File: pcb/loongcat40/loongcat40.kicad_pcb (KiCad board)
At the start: 2 copper layers, 83 parts, among them SW1 SW_Push, SW10 SW_Push, SW11 SW_Push, SW12 SW_Push, SW13 SW_Push, SW14 SW_Push, SW15 SW_Push, SW16 SW_Push, SW17 SW_Push, SW18 SW_Push, SW19 SW_Push, SW2 SW_Push, SW20 SW_Push, SW21 SW_Push, SW22 SW_Push, SW23 SW_Push, SW24 SW_Push, SW25 SW_Push, SW26 SW_Push, SW27 SW_Push, SW28 SW_Push, SW29 SW_Push, SW3 SW_Push, SW30 SW_Push, SW31 SW_Push, SW32 SW_Push, SW33 SW_Push, SW34 SW_Push, SW35 SW_Push, SW36 SW_Push, SW37 SW_Push, SW38 SW_Push, SW39 SW_Push, SW4 SW_Push, SW40 SW_Push, SW5 SW_Push, SW6 SW_Push, SW7 SW_Push, SW8 SW_Push, SW9 SW_Push

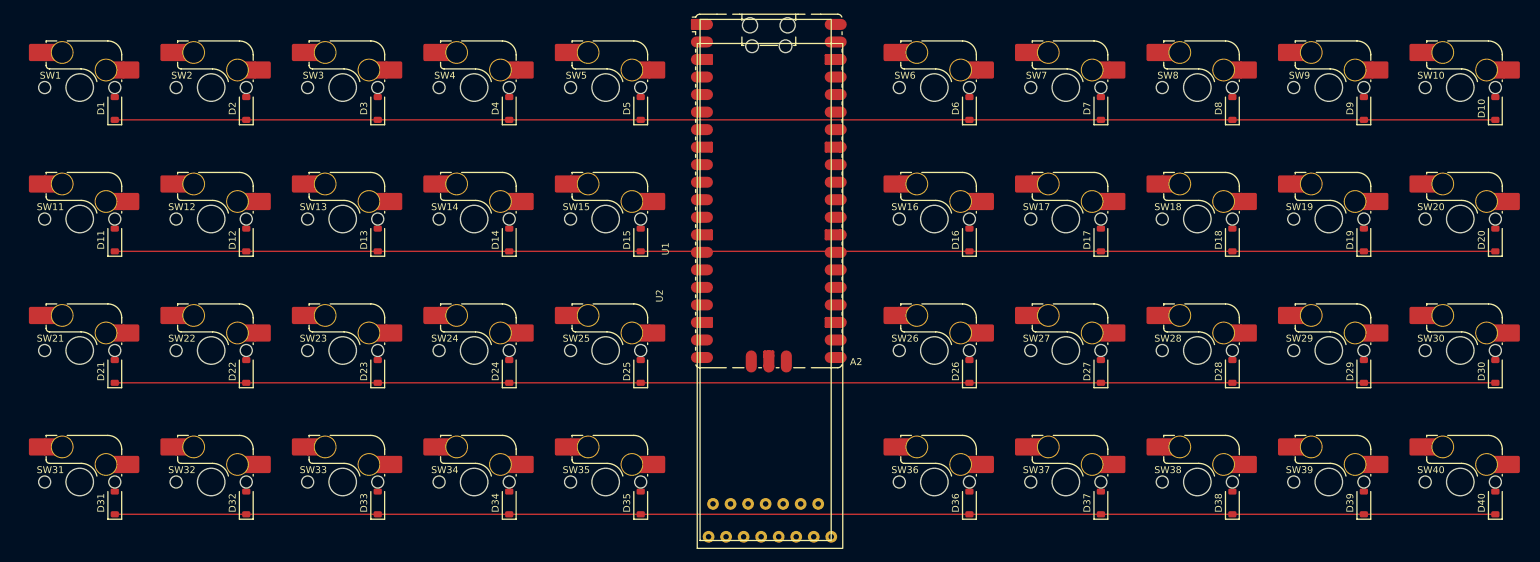
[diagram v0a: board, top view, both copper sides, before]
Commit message: position parts on pcb
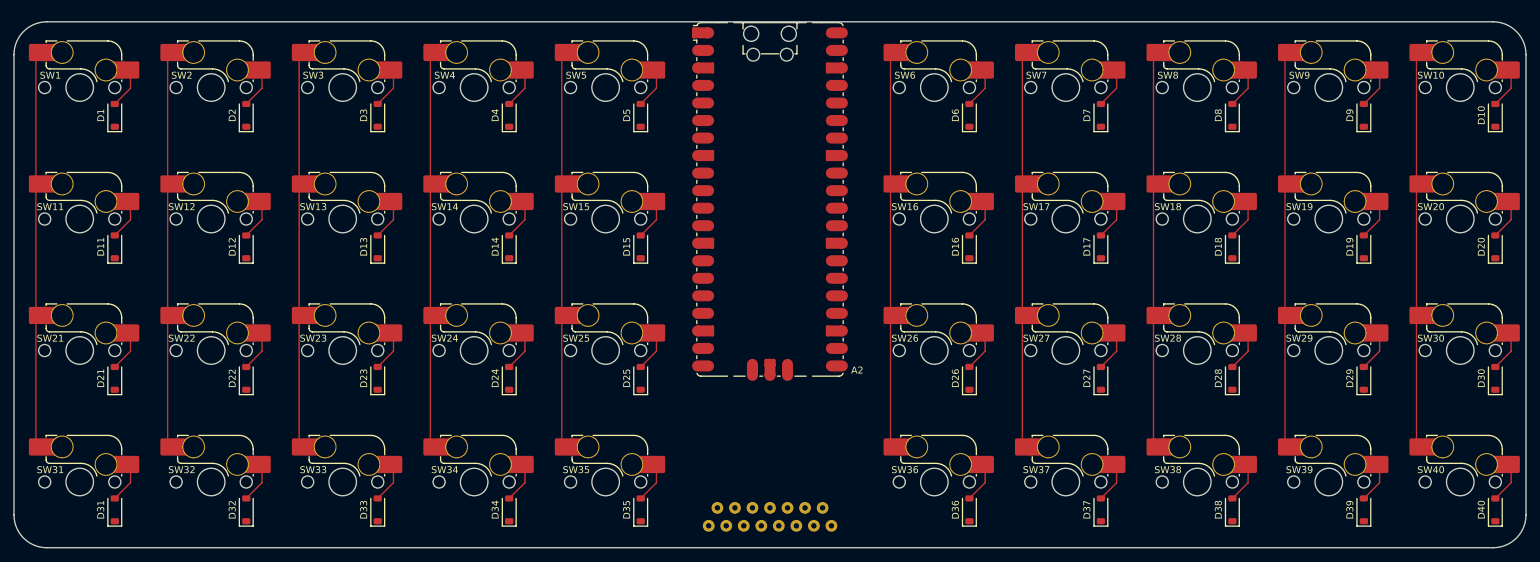
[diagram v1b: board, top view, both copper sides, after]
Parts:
- U1, U2: moved to B.Cu
- moved U2 1.59 mm to (138.1, 66.7)
- moved A2 1.23 mm to (138.1, 54.3)
- moved D1 1.00 mm to (43.2, 42.1)
- moved D10 1.00 mm to (243.2, 42.1)
- moved D11 1.00 mm to (43.2, 61.2)
- moved D12 1.00 mm to (62.2, 61.2)
- moved D13 1.00 mm to (81.3, 61.2)
- moved D14 1.00 mm to (100.3, 61.2)
- moved D15 1.00 mm to (119.4, 61.2)
- moved D16 1.00 mm to (167.0, 61.2)
- moved D17 1.00 mm to (186.1, 61.2)
- moved D18 1.00 mm to (205.1, 61.2)
- moved D19 1.00 mm to (224.2, 61.2)
- moved D2 1.00 mm to (62.2, 42.1)
- moved D20 1.00 mm to (243.2, 61.2)
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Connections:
- A2 pad 1: unconnected-(A2-GPIO0-Pad1) -> COL_1
- A2 pad 10: unconnected-(A2-GPIO7-Pad10) -> ROW_2
- A2 pad 11: unconnected-(A2-GPIO8-Pad11) -> ROW_3
- A2 pad 12: unconnected-(A2-GPIO9-Pad12) -> ROW_4
- A2 pad 19: unconnected-(A2-GPIO14-Pad19) -> RST
- A2 pad 2: unconnected-(A2-GPIO1-Pad2) -> COL_2
- A2 pad 20: unconnected-(A2-GPIO15-Pad20) -> DC
- A2 pad 22: unconnected-(A2-GPIO17-Pad22) -> CS
- A2 pad 24: unconnected-(A2-GPIO18-Pad24) -> SCL
- A2 pad 25: unconnected-(A2-GPIO19-Pad25) -> SDA
- A2 pad 26: unconnected-(A2-GPIO20-Pad26) -> COL_10
- A2 pad 27: unconnected-(A2-GPIO21-Pad27) -> COL_9
- A2 pad 29: unconnected-(A2-GPIO22-Pad29) -> COL_8
- A2 pad 31: unconnected-(A2-GPIO26_ADC0-Pad31) -> COL_7
- A2 pad 32: unconnected-(A2-GPIO27_ADC1-Pad32) -> COL_6
- A2 pad 4: unconnected-(A2-GPIO2-Pad4) -> COL_3
- A2 pad 5: unconnected-(A2-GPIO3-Pad5) -> COL_4
- A2 pad 6: unconnected-(A2-GPIO4-Pad6) -> COL_5
- A2 pad 9: unconnected-(A2-GPIO6-Pad9) -> ROW_1
- U2 pad 8: unconnected-(U2-BL-Pad8) -> BL
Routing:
- net ROW_4: track 200.0 -> 0.00 mm
- net ROW_2: track 200.0 -> 0.00 mm
- net ROW_3: track 200.0 -> 0.00 mm
- net ROW_1: track 200.0 -> 0.00 mm
- net COL_9: track 0.00 -> 57.4 mm
- net COL_6: track 0.00 -> 57.4 mm
- net COL_1: track 0.00 -> 57.4 mm
- net COL_8: track 0.00 -> 57.4 mm
- net COL_4: track 0.00 -> 57.4 mm
- net COL_10: track 0.00 -> 57.4 mm
- net COL_5: track 0.00 -> 57.4 mm
- net COL_2: track 0.00 -> 57.3 mm
- net COL_3: track 0.00 -> 57.3 mm
- net COL_7: track 0.00 -> 57.3 mm
- net Net-(D32-A): track 0.00 -> 5.86 mm
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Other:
- board outline added: 219.1 x 76.2 mm

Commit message: create outputs; init keyboard case
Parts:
- added H1: MountingHole_Pad, MountingHole:MountingHole_2.2mm_M2_Pad, F.Cu at (47.6, 47.6)
- added H2: MountingHole_Pad, MountingHole:MountingHole_2.2mm_M2_Pad, F.Cu at (228.6, 47.6)
- added H3: MountingHole_Pad, MountingHole:MountingHole_2.2mm_M2_Pad, F.Cu at (104.8, 66.7)
- added H4: MountingHole_Pad, MountingHole:MountingHole_2.2mm_M2_Pad, F.Cu at (171.4, 66.7)
- added H5: MountingHole_Pad, MountingHole:MountingHole_2.2mm_M2_Pad, F.Cu at (47.6, 85.7)
- added H6: MountingHole_Pad, MountingHole:MountingHole_2.2mm_M2_Pad, F.Cu at (228.6, 85.7)
- U2: moved to F.Cu
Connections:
- A2 pad 17: unconnected-(A2-GPIO13-Pad17) -> BL
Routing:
- net ROW_4: track 0.00 -> 272.5 mm, vias 0 -> 10
- net ROW_3: track 0.00 -> 256.3 mm, vias 0 -> 10
- net ROW_2: track 0.00 -> 239.0 mm, vias 0 -> 10
- net ROW_1: track 0.00 -> 232.8 mm, vias 0 -> 11
- net COL_1: track 57.4 -> 157.0 mm, vias 0 -> 2
- net COL_10: track 57.4 -> 144.2 mm, vias 0 -> 2
- net COL_2: track 57.3 -> 138.1 mm, vias 0 -> 2
- net COL_9: track 57.4 -> 122.4 mm, vias 0 -> 2
- net +3.3V: track 0.00 -> 63.2 mm, vias 0 -> 2
- net CS: track 0.00 -> 61.5 mm, vias 0 -> 4
- net BL: track 0.00 -> 60.2 mm, vias 0 -> 2
- net COL_3: track 57.3 -> 117.3 mm, vias 0 -> 2
- net SCL: track 0.00 -> 49.7 mm, vias 0 -> 4
- net COL_8: track 57.4 -> 104.1 mm, vias 0 -> 2
- net SDA: track 0.00 -> 44.5 mm, vias 0 -> 2
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- added copper zone on B.Cu, net +3.3V
- added copper zone on F.Cu, net GND
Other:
- board text added: "GND"
- board text added: "loongcat is looooooooooooooooooooooooooooooooooooooooooooooooooooooooooooooooooooooooooooooooooooooooooooooooooooooooooooooooooooooooooooooooooooooooooooooong"
- board text added: "loongcat40 v0.0 by sporewoh"

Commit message: update pcb to v0.1
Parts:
- added SW41: SW_Push, keyswitches:Kailh_socket_MX, B.Cu at (104.8, 95.2)
- added SW42: SW_Push, keyswitches:Kailh_socket_MX, B.Cu at (171.4, 95.2)
- A2: footprint Module:RaspberryPi_Pico_SMD_HandSolder -> Module:RaspberryPi_Pico_Common_Unspecified
- SW1, SW10, SW11, SW12, SW13, SW14, SW15, SW16, SW17, SW18, SW19, SW2, SW20, SW21, SW22, SW23, SW24, SW25, SW26, SW27, SW28, SW29, SW3, SW30, SW31, SW32, SW33, SW34, SW35, SW36, SW37, SW38, SW39, SW4, SW40, SW5, SW6, SW7, SW8, SW9: footprint marbastlib-mx:SW_MX_HS_CPG151101S11_1u -> keyswitches:Kailh_socket_MX; moved to B.Cu
- moved D34 9.84 mm to (90.5, 99.3)
- moved D36 8.25 mm to (158.8, 99.3)
- turned SW1 to 180 degrees
- turned SW10 to 180 degrees
- turned SW11 to 180 degrees
- turned SW12 to 180 degrees
- turned SW13 to 180 degrees
- turned SW14 to 180 degrees
- turned SW15 to 180 degrees
- turned SW16 to 180 degrees
- turned SW17 to 180 degrees
- turned SW18 to 180 degrees
- turned SW19 to 180 degrees
- turned SW2 to 180 degrees
- turned SW20 to 180 degrees
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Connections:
- SW1 pad 1: Net-(D1-A) -> COL_1
- SW1 pad 2: COL_1 -> Net-(D1-A)
- SW10 pad 1: Net-(D10-A) -> COL_10
- SW10 pad 2: COL_10 -> Net-(D10-A)
- SW11 pad 1: Net-(D11-A) -> COL_1
- SW11 pad 2: COL_1 -> Net-(D11-A)
- SW12 pad 1: Net-(D12-A) -> COL_2
- SW12 pad 2: COL_2 -> Net-(D12-A)
- SW13 pad 1: Net-(D13-A) -> COL_3
- SW13 pad 2: COL_3 -> Net-(D13-A)
- SW14 pad 1: Net-(D14-A) -> COL_4
- SW14 pad 2: COL_4 -> Net-(D14-A)
- SW15 pad 1: Net-(D15-A) -> COL_5
- SW15 pad 2: COL_5 -> Net-(D15-A)
- SW16 pad 1: Net-(D16-A) -> COL_6
- SW16 pad 2: COL_6 -> Net-(D16-A)
- SW17 pad 1: Net-(D17-A) -> COL_7
- SW17 pad 2: COL_7 -> Net-(D17-A)
- SW18 pad 1: Net-(D18-A) -> COL_8
- SW18 pad 2: COL_8 -> Net-(D18-A)
- SW19 pad 1: Net-(D19-A) -> COL_9
- SW19 pad 2: COL_9 -> Net-(D19-A)
- SW2 pad 1: Net-(D2-A) -> COL_2
- SW2 pad 2: COL_2 -> Net-(D2-A)
- SW20 pad 1: Net-(D20-A) -> COL_10
- SW20 pad 2: COL_10 -> Net-(D20-A)
- SW21 pad 1: Net-(D21-A) -> COL_1
- SW21 pad 2: COL_1 -> Net-(D21-A)
- SW22 pad 1: Net-(D22-A) -> COL_2
- SW22 pad 2: COL_2 -> Net-(D22-A)
- SW23 pad 1: Net-(D23-A) -> COL_3
- SW23 pad 2: COL_3 -> Net-(D23-A)
- SW24 pad 1: Net-(D24-A) -> COL_4
- SW24 pad 2: COL_4 -> Net-(D24-A)
- SW25 pad 1: Net-(D25-A) -> COL_5
- SW25 pad 2: COL_5 -> Net-(D25-A)
- SW26 pad 1: Net-(D26-A) -> COL_6
- SW26 pad 2: COL_6 -> Net-(D26-A)
- SW27 pad 1: Net-(D27-A) -> COL_7
- SW27 pad 2: COL_7 -> Net-(D27-A)
- SW28 pad 1: Net-(D28-A) -> COL_8
- SW28 pad 2: COL_8 -> Net-(D28-A)
- SW29 pad 1: Net-(D29-A) -> COL_9
- SW29 pad 2: COL_9 -> Net-(D29-A)
- SW3 pad 1: Net-(D3-A) -> COL_3
- SW3 pad 2: COL_3 -> Net-(D3-A)
- SW30 pad 1: Net-(D30-A) -> COL_10
- SW30 pad 2: COL_10 -> Net-(D30-A)
- SW31 pad 1: Net-(D31-A) -> COL_1
- SW31 pad 2: COL_1 -> Net-(D31-A)
- SW32 pad 1: Net-(D32-A) -> COL_2
- SW32 pad 2: COL_2 -> Net-(D32-A)
- SW33 pad 1: Net-(D33-A) -> COL_3
- SW33 pad 2: COL_3 -> Net-(D33-A)
- SW34 pad 1: Net-(D34-A) -> COL_4
- SW34 pad 2: COL_4 -> Net-(D34-A)
- SW35 pad 1: Net-(D35-A) -> COL_5
- SW35 pad 2: COL_5 -> Net-(D35-A)
- SW36 pad 1: Net-(D36-A) -> COL_6
- SW36 pad 2: COL_6 -> Net-(D36-A)
- SW37 pad 1: Net-(D37-A) -> COL_7
- SW37 pad 2: COL_7 -> Net-(D37-A)
- SW38 pad 1: Net-(D38-A) -> COL_8
- SW38 pad 2: COL_8 -> Net-(D38-A)
- SW39 pad 1: Net-(D39-A) -> COL_9
- SW39 pad 2: COL_9 -> Net-(D39-A)
- SW4 pad 1: Net-(D4-A) -> COL_4
- SW4 pad 2: COL_4 -> Net-(D4-A)
- SW40 pad 1: Net-(D40-A) -> COL_10
- SW40 pad 2: COL_10 -> Net-(D40-A)
- SW5 pad 1: Net-(D5-A) -> COL_5
- SW5 pad 2: COL_5 -> Net-(D5-A)
- SW6 pad 1: Net-(D6-A) -> COL_6
- SW6 pad 2: COL_6 -> Net-(D6-A)
- SW7 pad 1: Net-(D7-A) -> COL_7
- SW7 pad 2: COL_7 -> Net-(D7-A)
- SW8 pad 1: Net-(D8-A) -> COL_8
- SW8 pad 2: COL_8 -> Net-(D8-A)
- SW9 pad 1: Net-(D9-A) -> COL_9
- SW9 pad 2: COL_9 -> Net-(D9-A)
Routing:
- net COL_6: track 66.3 -> 98.9 mm, vias 2 -> 4
- net Net-(D35-A): track 5.86 -> 29.6 mm, vias 0 -> 2
- net Net-(D36-A): track 5.86 -> 19.1 mm
- net COL_5: track 78.5 -> 89.9 mm
- net Net-(D34-A): track 5.86 -> 16.4 mm
- net GND: track 2.01 -> 0.00 mm
- net ROW_1: track 232.8 -> 233.5 mm
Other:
- board text added: "loongcat40 v0.1 by sporewoh"
- board text removed: "loongcat40 v0.0 by sporewoh"

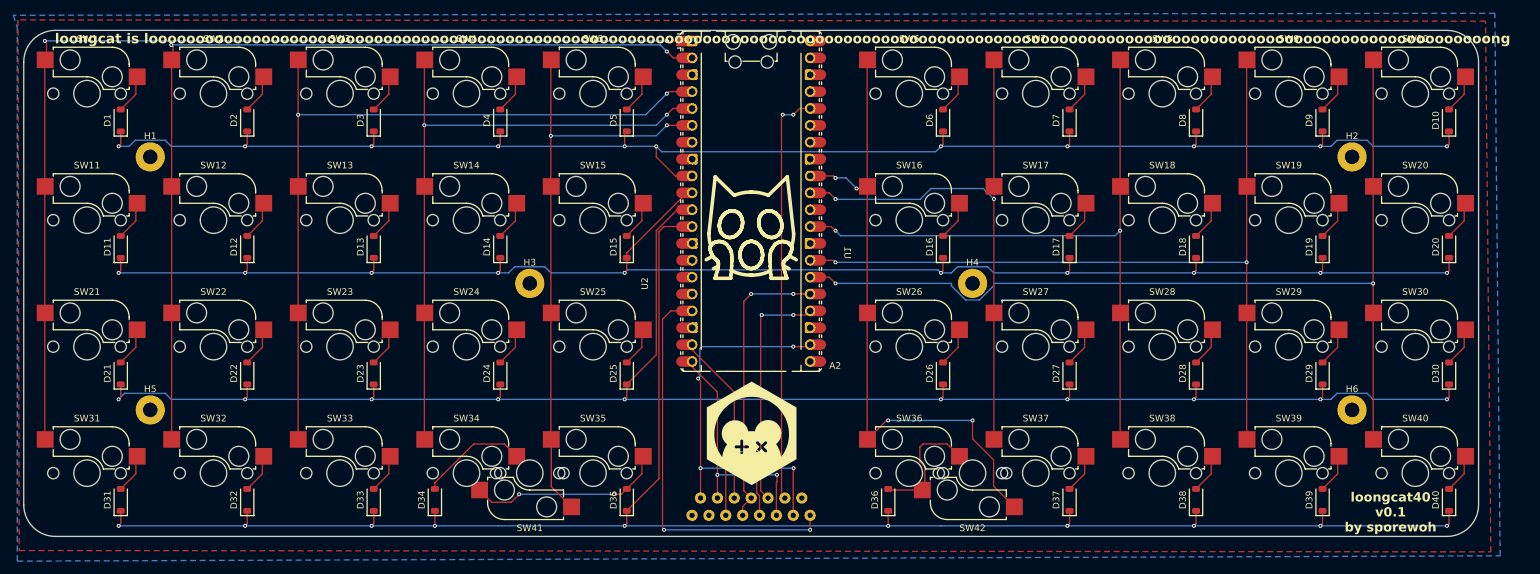
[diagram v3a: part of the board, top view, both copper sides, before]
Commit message: reduce ground plane
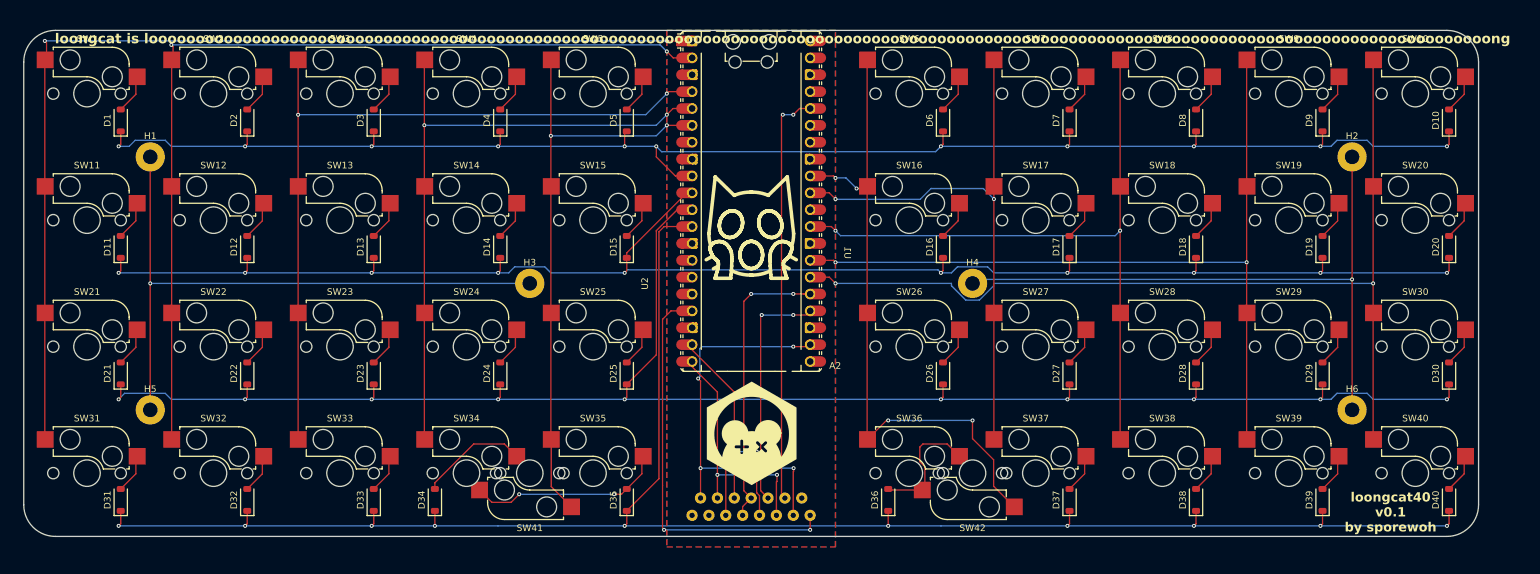
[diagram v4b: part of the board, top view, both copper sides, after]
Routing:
- net GND: track 0.00 -> 190.7 mm, vias 0 -> 2
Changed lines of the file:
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@@
 	)
 	(segment
+		(start 228.6 47.625)
+		(end 228.6 85.725)
+		(width 0.2)
+		(layer "F.Cu")
+		(net 1)
+	)
+	(segment
+		(start 47.625 47.625)
+		(end 47.625 66.675)
+		(width 0.2)
+		(layer "F.Cu")
+		(net 1)
+	)
+	(segment
+		(start 47.625 66.675)
+		(end 47.625 85.725)
+		(width 0.2)
+		(layer "F.Cu")
+		(net 1)
+	)
+	(via
+		(at 228.6 66.075)
+		(size 0.6)
+		(drill 0.3)
+		(layers "F.Cu" "B.Cu")
+		(net 1)
+	)
+	(via
+		(at 47.625 66.675)
+		(size 0.6)
+		(drill 0.3)
+		(layers "F.Cu" "B.Cu")
+		(net 1)
+	)
+	(segment
+		(start 172.05 66.075)
+		(end 228.6 66.075)
+		(width 0.2)
+		(layer "B.Cu")
+		(net 1)
+	)
+	(segment
+		(start 104.775 66.675)
+		(end 47.625 66.675)
+		(width 0.2)
+		(layer "B.Cu")
+		(net 1)
+	)
+	(segment
+		(start 171.45 66.675)
+		(end 172.05 66.075)
+		(width 0.2)
+		(layer "B.Cu")
+		(net 1)
+	)
+	(segment
 		(start 142.683519 98.491019)
 		(end 143.1925 99)
@@
 		(polygon
 			(pts
-				(xy 27.7 27) (xy 27.9 106.9) (xy 249.5 107.1) (xy 248.7 27.2)
+				(xy 125.4125 28.575) (xy 125.4125 106.3625) (xy 150.8125 106.3625) (xy 150.8125 28.575)
 			)
 		)
@@
 		(polygon
 			(pts
-				(xy 27.6 28.1) (xy 27.6 108.5) (xy 250.9 107.7) (xy 250.1 26) (xy 27 26.3)
+				(xy 125.4125 28.575) (xy 125.4125 106.3625) (xy 150.8125 106.3625) (xy 150.8125 28.575) (xy 125.4125 28.575)
 			)
 		)

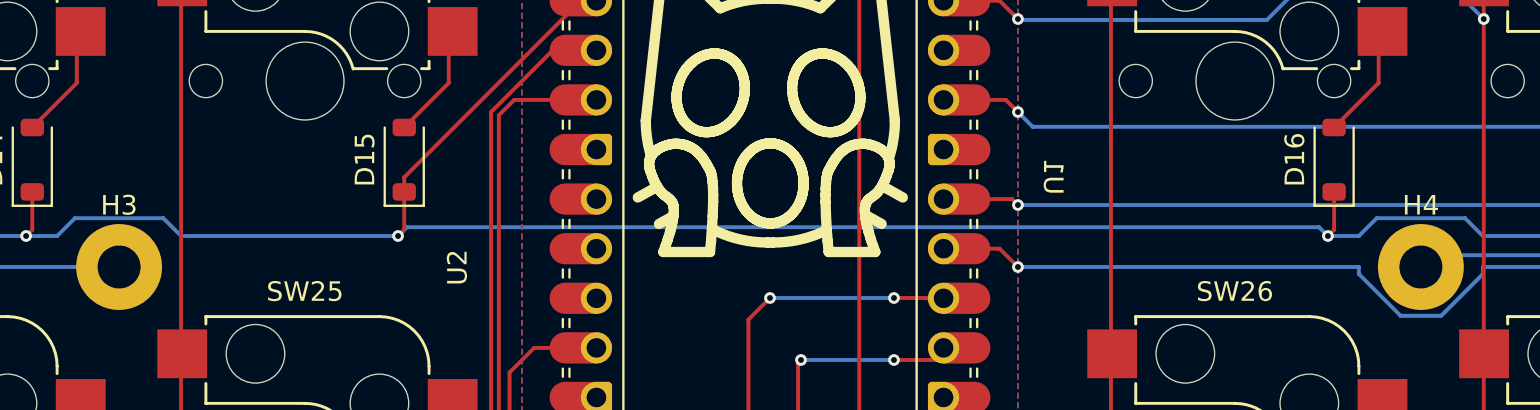
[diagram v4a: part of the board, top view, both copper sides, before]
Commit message: connect ground holes to pico
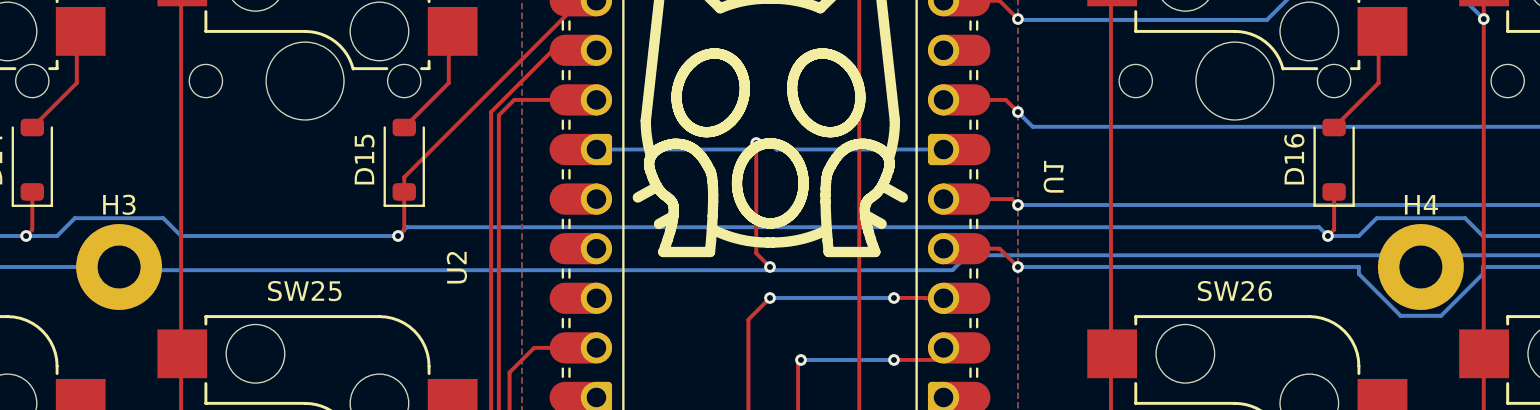
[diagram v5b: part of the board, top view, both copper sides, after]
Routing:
- net GND: track 190.7 -> 282.9 mm, vias 2 -> 4
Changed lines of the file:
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@@
 		(net 1)
 	)
+	(segment
+		(start 138.1125 66.675)
+		(end 137.4092 65.9717)
+		(width 0.2)
+		(layer "F.Cu")
+		(net 1)
+	)
+	(segment
+		(start 137.4092 65.9717)
+		(end 137.4092 60.324764)
+		(width 0.2)
+		(layer "F.Cu")
+		(net 1)
+	)
+	(via
+		(at 138.1125 66.675)
+		(size 0.6)
+		(drill 0.3)
+		(layers "F.Cu" "B.Cu")
+		(net 1)
+	)
 	(via
 		(at 228.6 66.075)
@@
 		(net 1)
 	)
+	(via
+		(at 137.4092 60.324764)
+		(size 0.6)
+		(drill 0.3)
+		(layers "F.Cu" "B.Cu")
+		(net 1)
+	)
+	(segment
+		(start 138.112264 60.324764)
+		(end 138.445 60.6575)
+		(width 0.2)
+		(layer "B.Cu")
+		(net 1)
+	)
+	(segment
+		(start 129.2225 60.6575)
+		(end 137.076464 60.6575)
+		(width 0.2)
+		(layer "B.Cu")
+		(net 1)
+	)
+	(segment
+		(start 138.1125 66.675)
+		(end 137.949 66.8385)
+		(width 0.2)
+		(layer "B.Cu")
+		(net 1)
+	)
 	(segment
 		(start 172.05 66.075)
@@
 	)
 	(segment
+		(start 104.9385 66.8385)
+		(end 104.775 66.675)
+		(width 0.2)
+		(layer "B.Cu")
+		(net 1)
+	)
+	(segment
+		(start 137.076464 60.6575)
+		(end 137.4092 60.324764)
+		(width 0.2)
+		(layer "B.Cu")
+		(net 1)
+	)
+	(segment
+		(start 147.45855 66.8385)
+		(end 138.276 66.8385)
+		(width 0.2)
+		(layer "B.Cu")
+		(net 1)
+	)
+	(segment
+		(start 137.4092 60.324764)
+		(end 138.112264 60.324764)
+		(width 0.2)
+		(layer "B.Cu")
+		(net 1)
+	)
+	(segment
+		(start 148.22305 66.074)
+		(end 147.45855 66.8385)
+		(width 0.2)
+		(layer "B.Cu")
+		(net 1)
+	)
+	(segment
+		(start 170.849 66.074)
+		(end 148.22305 66.074)
+		(width 0.2)
+		(layer "B.Cu")
+		(net 1)
+	)
+	(segment
+		(start 138.445 60.6575)
+		(end 147.0025 60.6575)
+		(width 0.2)
+		(layer "B.Cu")
+		(net 1)
+	)
+	(segment
 		(start 104.775 66.675)
 		(end 47.625 66.675)
@@
 	(segment
 		(start 171.45 66.675)
+		(end 170.849 66.074)
+		(width 0.2)
+		(layer "B.Cu")
+		(net 1)
+	)
+	(segment
+		(start 171.45 66.675)
 		(end 172.05 66.075)
 		(width 0.2)
@@
 	)
 	(segment
+		(start 138.276 66.8385)
+		(end 138.1125 66.675)
+		(width 0.2)
+		(layer "B.Cu")
+		(net 1)
+	)
+	(segment
+		(start 137.949 66.8385)
+		(end 104.9385 66.8385)
+		(width 0.2)
+		(layer "B.Cu")
+		(net 1)
+	)
+	(segment
 		(start 142.683519 98.491019)
 		(end 143.1925 99)
@@
 		(polygon
 			(pts
-				(xy 125.4125 28.575) (xy 125.4125 106.3625) (xy 150.8125 106.3625) (xy 150.8125 28.575) (xy 125.4125 28.575)
+				(xy 125.4125 28.575) (xy 125.4125 106.3625) (xy 150.8125 106.3625) (xy 150.8125 28.575)
 			)
 		)
